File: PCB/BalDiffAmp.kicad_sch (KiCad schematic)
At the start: 15 parts, among them U11 OPA1622

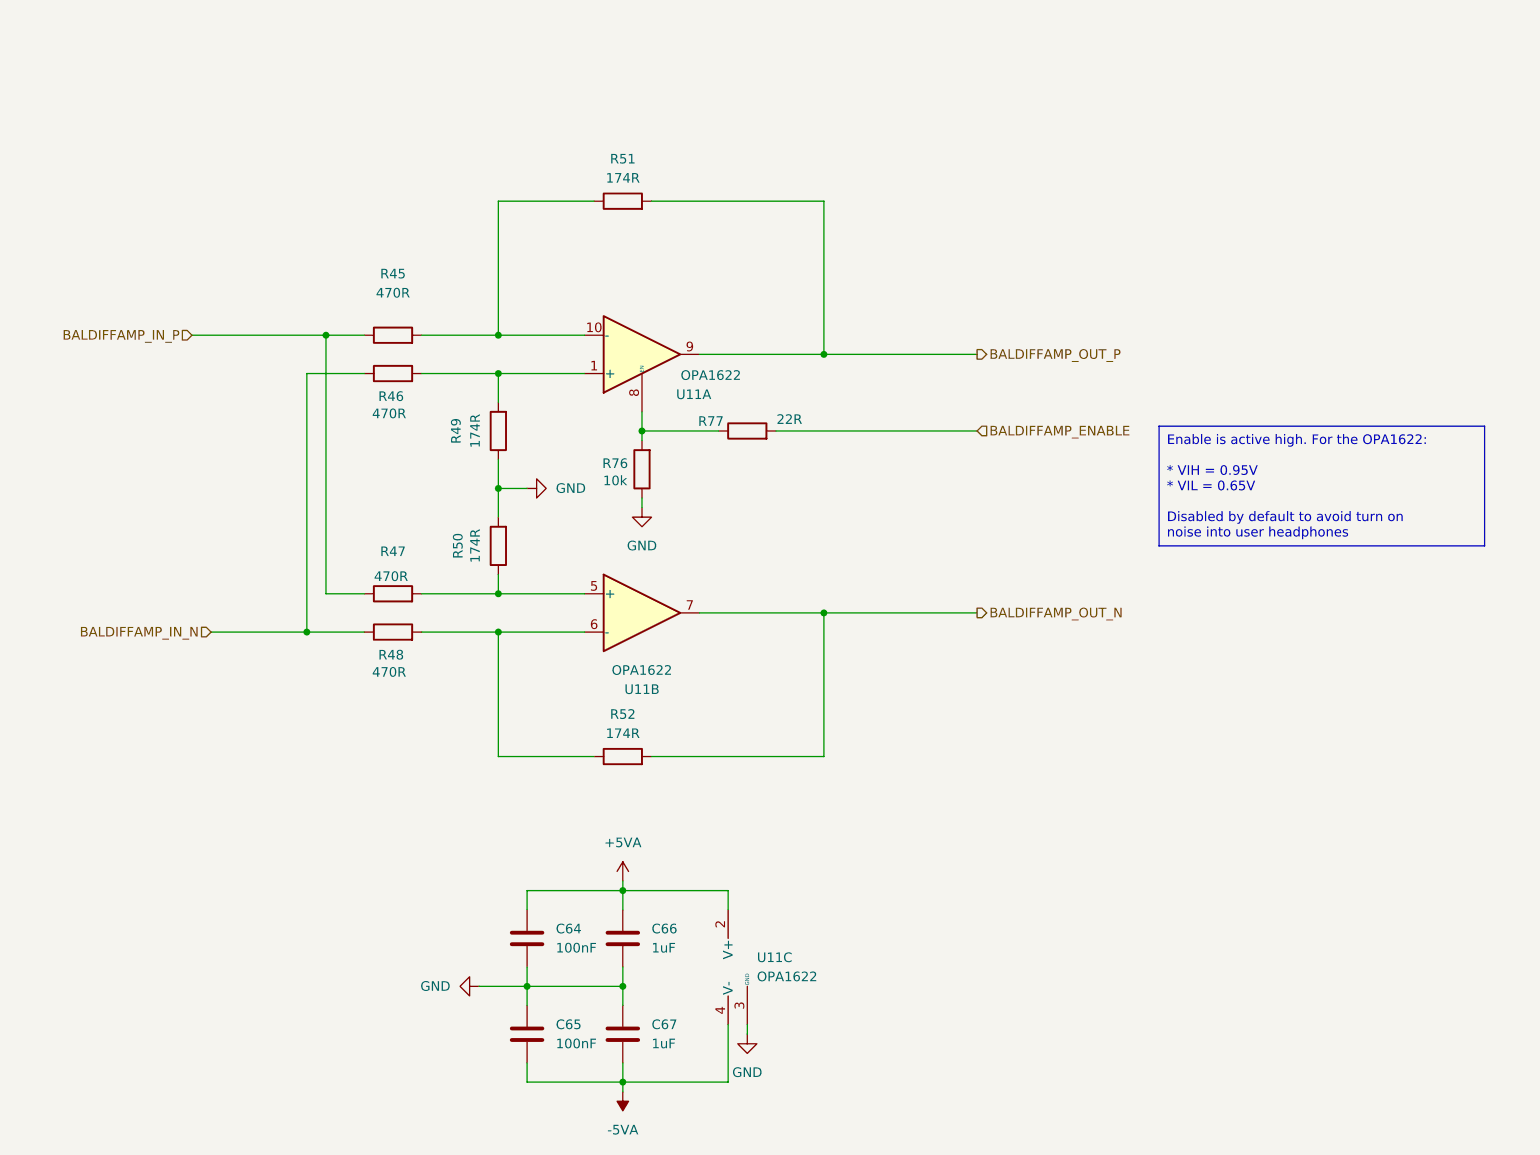
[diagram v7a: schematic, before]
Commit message: Added filter capacitors to OPA1622 circuitry
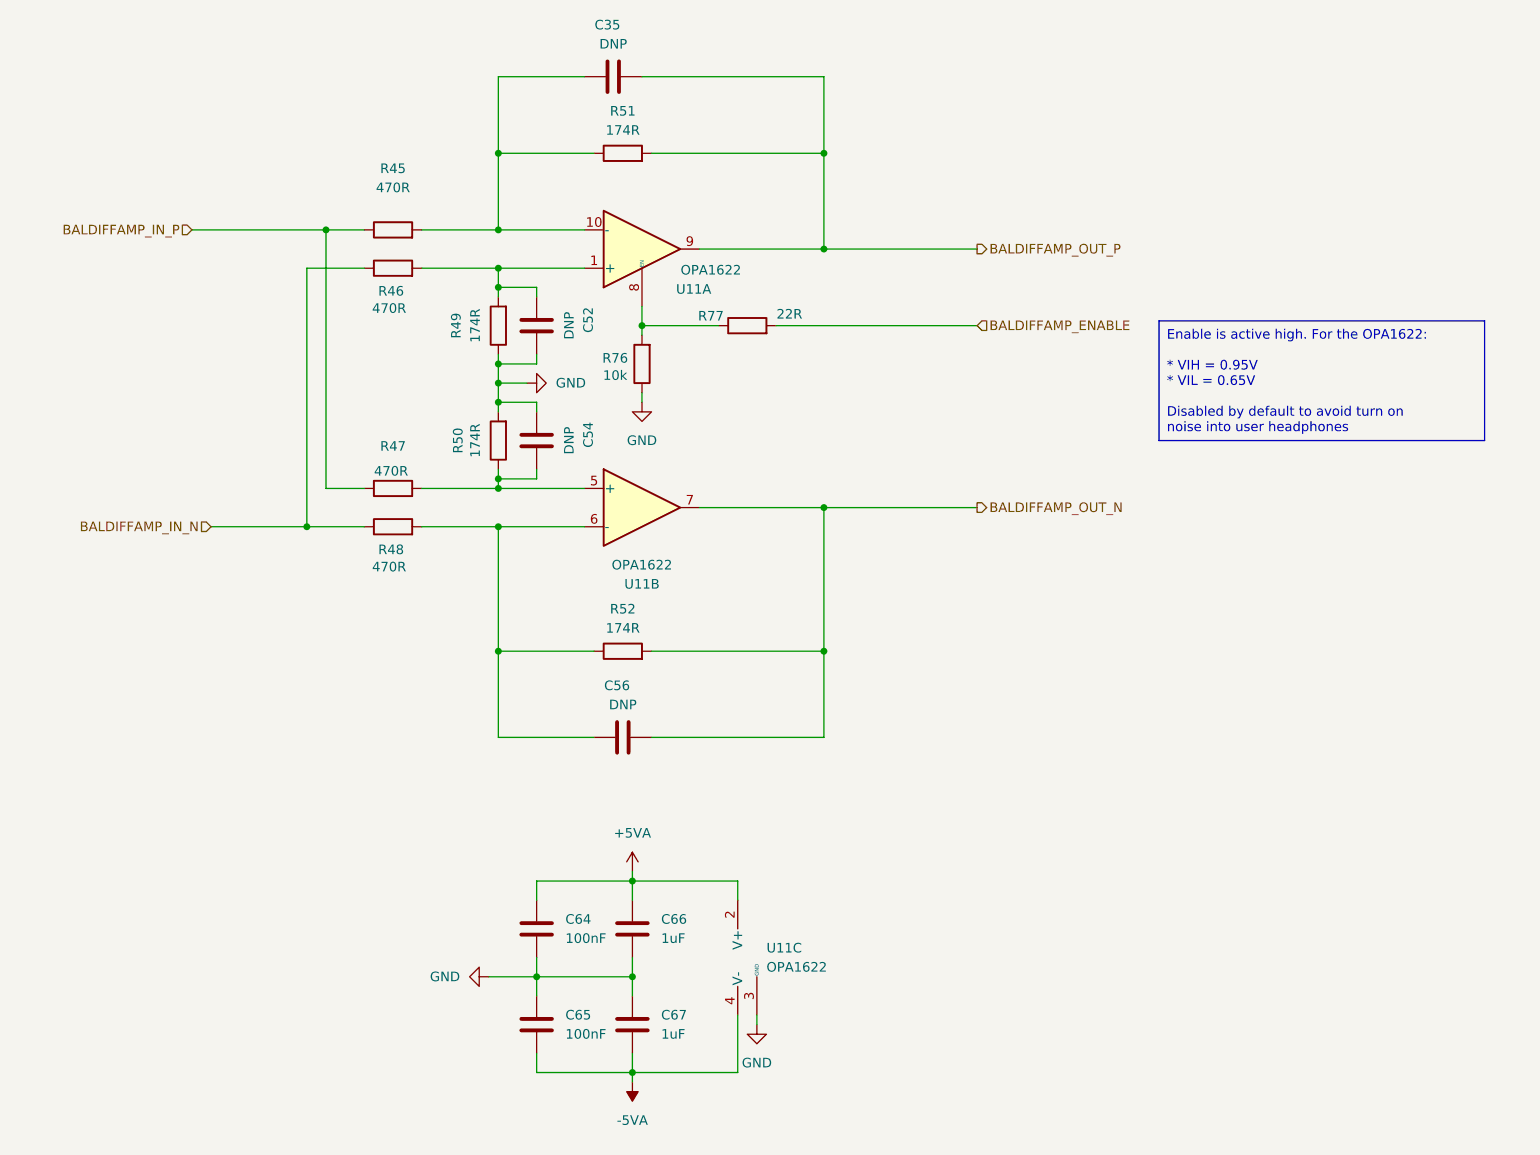
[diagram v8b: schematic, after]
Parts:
- added C35, C52, C54, C56: DNP, Capacitor_SMD:C_0603_1608Metric_Pad1.08x0.95mm_HandSolder, symbol Device:C
- C64, C65: JLCPCBPn C1525 -> (none); LCSC Part # (none) -> C1525
- C66, C67: JLCPCBPn C15849 -> (none); LCSC Part # (none) -> C15849
- R45, R46, R47, R48: JLCPCBPn C445590 -> (none); LCSC Part # (none) -> C445590
- R49, R50, R51, R52: JLCPCBPn C852566 -> (none); LCSC Part # (none) -> C852566
- R76: JLCPCBPn C25744 -> (none); LCSC Part # (none) -> C25744
- R77: JLCPCBPn C25092 -> (none); LCSC Part # (none) -> C25092
- U11: JLCPCBPn C2876559 -> (none); LCSC Part # (none) -> C2876559
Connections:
- net BALDIFFAMP_OUT_N: now also C56.2
- net BALDIFFAMP_OUT_P: now also C35.2
- net GND: now also C52.2, C54.1
- net at R45.2, R51.1, U11.10 (-): now also C35.1
- net at R47.2, R50.1, U11.5 (+): now also C54.2
- net at R48.2, R52.1, U11.6 (-): now also C56.1
- net at R46.2, R49.2, U11.1 (+): now also C52.1
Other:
- moved on the sheet: C64, C65, C66, C67, R45, R46, R47, R48, R49, R50, R51, R52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
